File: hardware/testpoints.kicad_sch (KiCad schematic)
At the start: 29 parts, among them J3 Conn_01x04

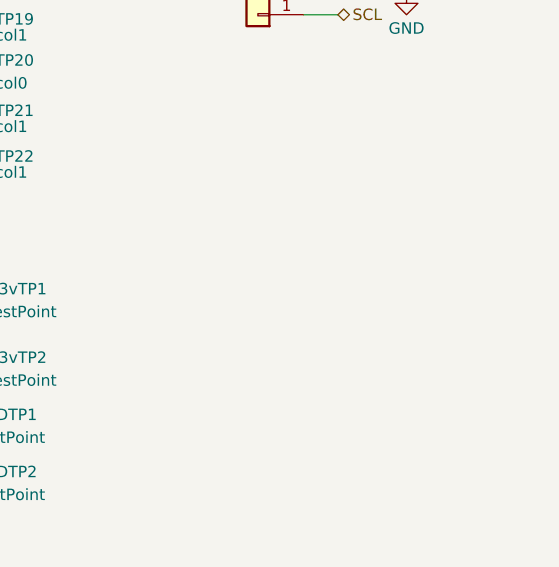
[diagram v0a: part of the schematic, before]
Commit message: production files added --> ready for assembly
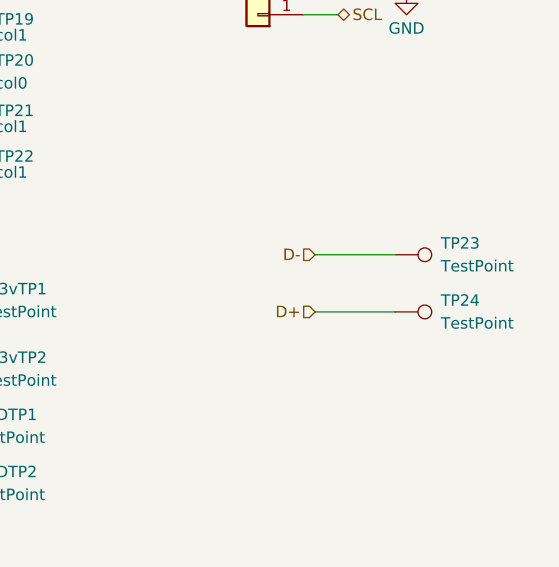
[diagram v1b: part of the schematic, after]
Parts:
- added TP23, TP24: TestPoint, TestPoint:TestPoint_THTPad_1.0x1.0mm_Drill0.5mm, symbol Connector:TestPoint
- 3.3vTP1, 3.3vTP2, 5vTP1, GNDTP1, GNDTP2, J3, TP1, TP10, TP11, TP12, TP13, TP14, TP15, TP16, TP17, TP18, TP19, TP2, TP20, TP21, TP22, TP3, TP4, TP5, TP6, TP7, TP8, TP9, VBUSTP1: now left out of the parts list
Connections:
- new net D+: TP24.1
- new net D-: TP23.1
